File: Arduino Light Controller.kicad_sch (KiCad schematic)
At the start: 44 parts, among them J1 Terminal - Pin - Male - 1x2 -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, J10 Terminal - Pin - Male - 1x2 -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, J11 Terminal - Pin - Male - 1x2 -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, J12 Terminal - Pin - Male - 1x2 -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, J13 Terminal - Pin - Male - 1x2 -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, J14 Terminal - Pin - Male - 1x2 -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, J15 Terminal - Pin - Male - 1x2 -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, J16 Terminal - Pin - Male - 1x2 -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, J17 Terminal - Pin - Male - 1x2 -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, J18 Terminal - Pin - Male - 1x2 -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, J19 Terminal - Pin - Male - 1x4 -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, J2 Terminal - Pin - Male - 1x2 -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, J20 Terminal - Pin - Male - 1x4 -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, J21 Terminal - Pin - Male - 1x4 -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, J22 Terminal - Pin - Male - 1x4 -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, J3 Terminal - Pin - Male - 1x2 -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, J4 Terminal - Pin - Male - 1x2 -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, J5 Terminal - Pin - Male - 1x2 -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, J6 Terminal - Pin - Male - 1x2 -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, J7 Terminal - Pin - Male - 1x2 -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, J8 Terminal - Pin - Male - 1x2 -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, J9 Terminal - Pin - Male - 1x2 -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

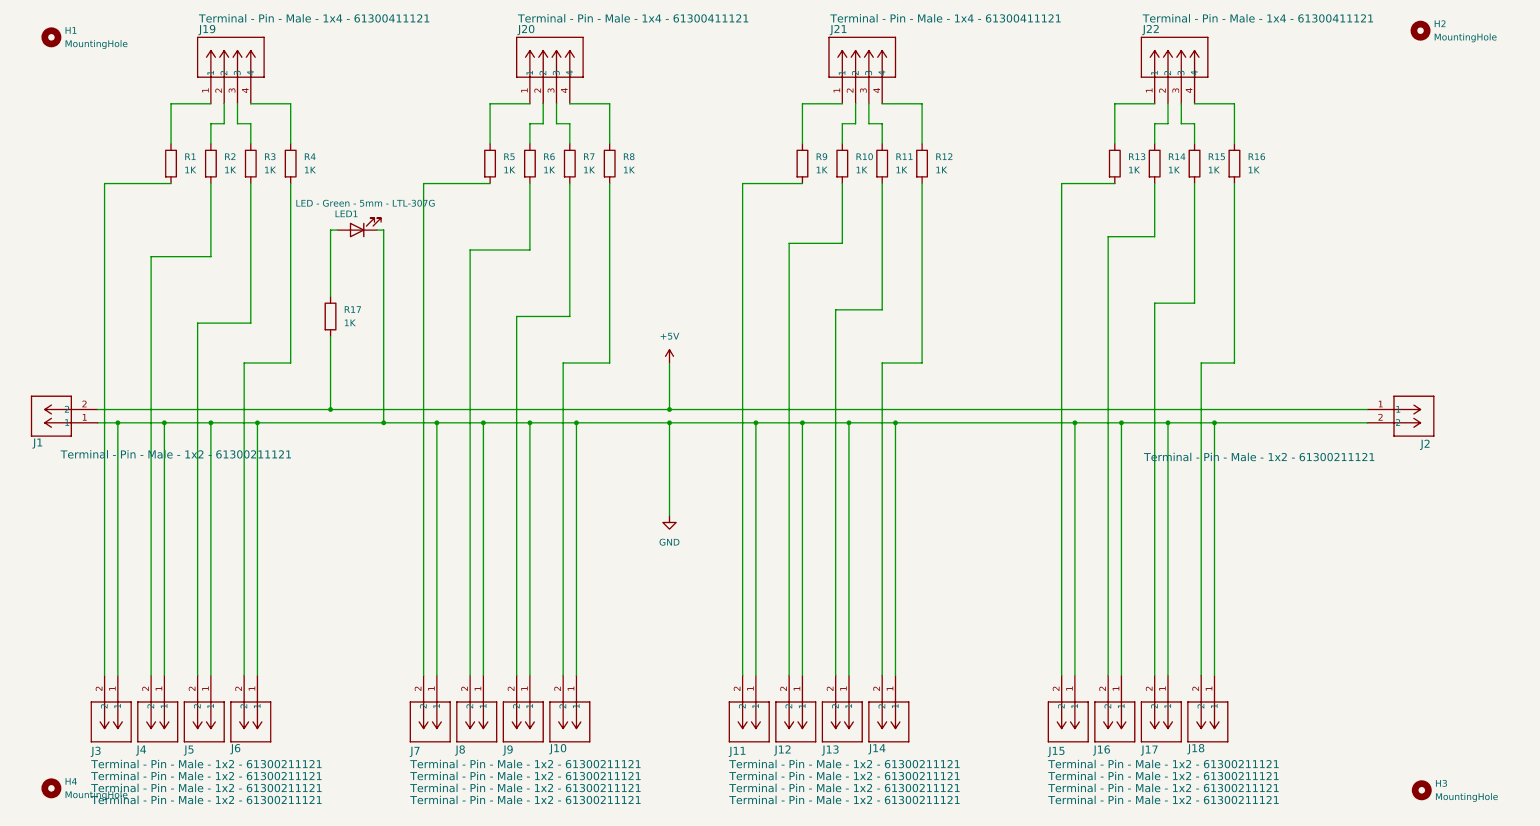
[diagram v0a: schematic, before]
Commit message: New design to align with other boards and support power bus.
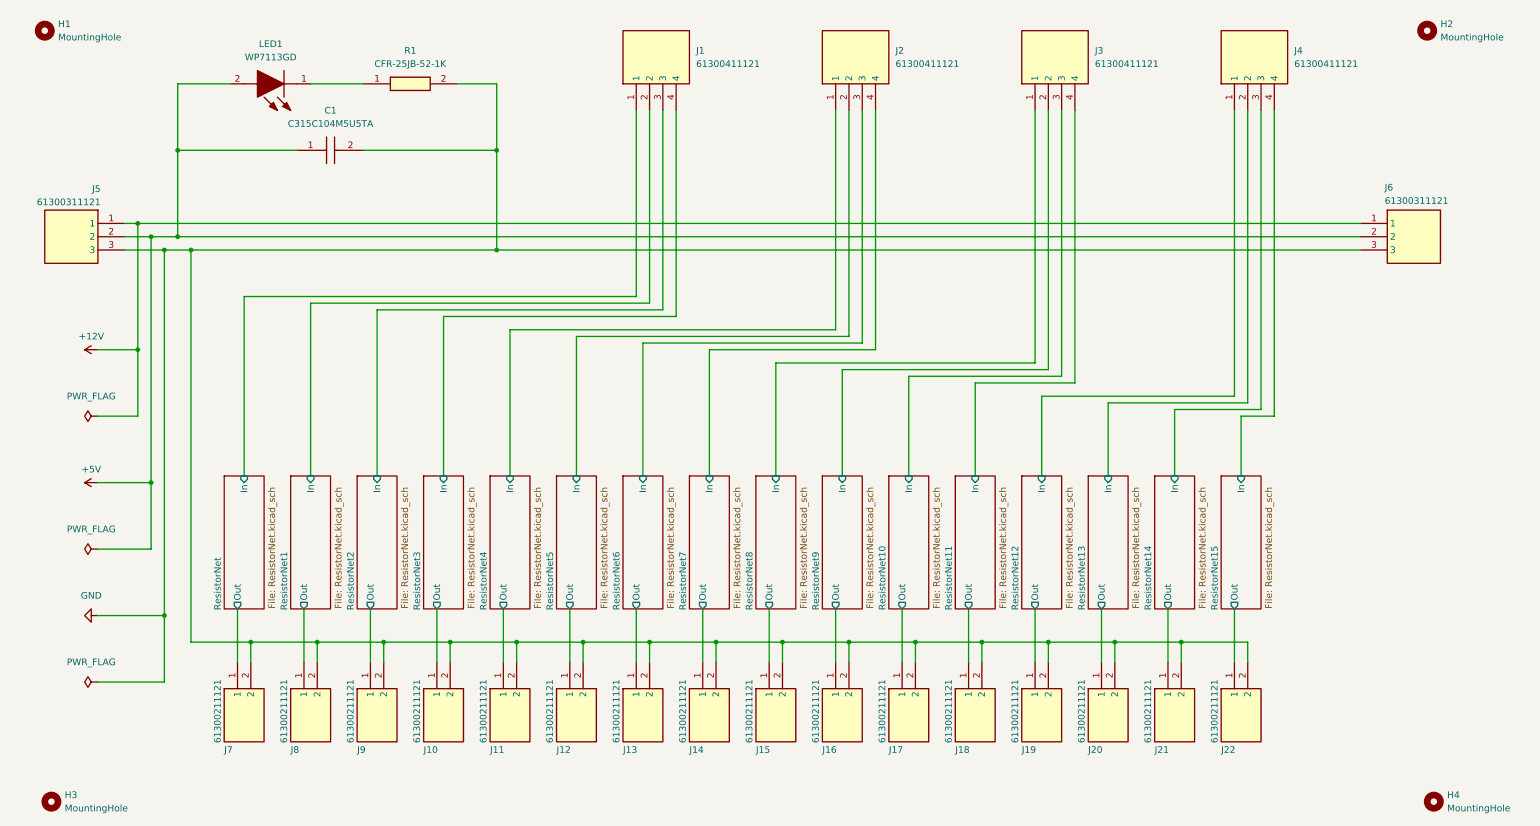
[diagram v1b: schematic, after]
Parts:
- removed J1, J10, J11, J12, J13, J14, J15, J16, J17, J18, J2, J3, J4, J5, J6, J7, J8, J9: Terminal - Pin - Male - 1x2 - 61300211121, Digikey:Terminal - Pin - Male - 1x2 - 61300211121, symbol Digikey:Terminal - Pin - Male - 1x2 - 61300211121
- removed J19, J20, J21, J22: Terminal - Pin - Male - 1x4 - 61300411121, Digikey:Terminal - Pin - Male - 1x4 - 61300411121, symbol Digikey:Terminal - Pin - Male - 1x4 - 61300411121
- removed LED1: LED - Green - 5mm - LTL-307G, Digikey:LED - Green - 5mm - LTL-307G, symbol Digikey:LED - Green - 5mm - LTL-307G
- removed R1, R10, R11, R12, R13, R14, R15, R16, R17, R2, R3, R4, R5, R6, R7, R8, R9: 1K, Resistor_THT:R_Axial_DIN0204_L3.6mm_D1.6mm_P7.62mm_Horizontal, symbol Digikey:Resistor - Generic
- added C1: C315C104M5U5TA, SamacSys_Parts:C315C100J2G5TA, symbol SamacSys_Parts:C315C104M5U5TA
- added J1, J2, J3, J4: 61300411121, SamacSys_Parts:HDRV4W95P0X254_1X4_1016X254X854P, symbol SamacSys_Parts:61300411121
- added J10, J11, J12, J13, J14, J15, J16, J17, J18, J19, J20, J21, J22, J7, J8, J9: 61300211121, SamacSys_Parts:HDRV2W110P0X254_1X2_508X254X854P, symbol SamacSys_Parts:61300211121
- added J5, J6: 61300311121, SamacSys_Parts:HDRV3W64P0X254_1X3_762X254X869P, symbol SamacSys_Parts:61300311121
- added LED1: WP7113GD, SamacSys_Parts:L53ND, symbol SamacSys_Parts:WP7113GD
- added R1: CFR-25JB-52-1K, SamacSys_Parts:RESAD1590W60L630D240, symbol SamacSys_Parts:CFR-25JB-52-1K
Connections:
- net +5V: now also C1.1, J5.2, J6.2, LED1.2 (A)
- net GND: now also C1.2, J10.2, J11.2, J12.2, J13.2, J14.2, J15.2, J16.2, J17.2, J18.2, J19.2, J20.2, J21.2, J22.2, J5.3, J6.3, J7.2, J8.2, J9.2, R1.2
- new net: LED1.1 (K), R1.1
- new net +12V: J5.1, J6.1
- new net ResistorNet/In: J1.1
- new net ResistorNet/Out: J7.1
- new net ResistorNet1/In: J1.2
- new net ResistorNet1/Out: J8.1
- new net ResistorNet10/In: J3.3
- new net ResistorNet10/Out: J17.1
- new net ResistorNet11/In: J3.4
- new net ResistorNet11/Out: J18.1
- new net ResistorNet12/In: J4.1
- new net ResistorNet12/Out: J19.1
- new net ResistorNet13/In: J4.2
- new net ResistorNet13/Out: J20.1
- new net ResistorNet14/In: J4.3
- new net ResistorNet14/Out: J21.1
- new net ResistorNet15/In: J4.4
- new net ResistorNet15/Out: J22.1
- new net ResistorNet2/In: J1.3
- new net ResistorNet2/Out: J9.1
- new net ResistorNet3/In: J1.4
- new net ResistorNet3/Out: J10.1
- new net ResistorNet4/In: J2.1
- new net ResistorNet4/Out: J11.1
- new net ResistorNet5/In: J2.2
- new net ResistorNet5/Out: J12.1
- new net ResistorNet6/In: J2.3
- new net ResistorNet6/Out: J13.1
- new net ResistorNet7/In: J2.4
- new net ResistorNet7/Out: J14.1
- new net ResistorNet8/In: J3.1
- new net ResistorNet8/Out: J15.1
- new net ResistorNet9/In: J3.2
- new net ResistorNet9/Out: J16.1
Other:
- added sheet ResistorNet (ResistorNet.kicad_sch)
- added sheet ResistorNet1 (ResistorNet.kicad_sch)
- added sheet ResistorNet10 (ResistorNet.kicad_sch)
- added sheet ResistorNet11 (ResistorNet.kicad_sch)
- added sheet ResistorNet12 (ResistorNet.kicad_sch)
- added sheet ResistorNet13 (ResistorNet.kicad_sch)
- added sheet ResistorNet14 (ResistorNet.kicad_sch)
- added sheet ResistorNet15 (ResistorNet.kicad_sch)
- added sheet ResistorNet2 (ResistorNet.kicad_sch)
- added sheet ResistorNet3 (ResistorNet.kicad_sch)
- added sheet ResistorNet4 (ResistorNet.kicad_sch)
- added sheet ResistorNet5 (ResistorNet.kicad_sch)
- added sheet ResistorNet6 (ResistorNet.kicad_sch)
- added sheet ResistorNet7 (ResistorNet.kicad_sch)
- added sheet ResistorNet8 (ResistorNet.kicad_sch)
- added sheet ResistorNet9 (ResistorNet.kicad_sch)
- moved on the sheet: H1

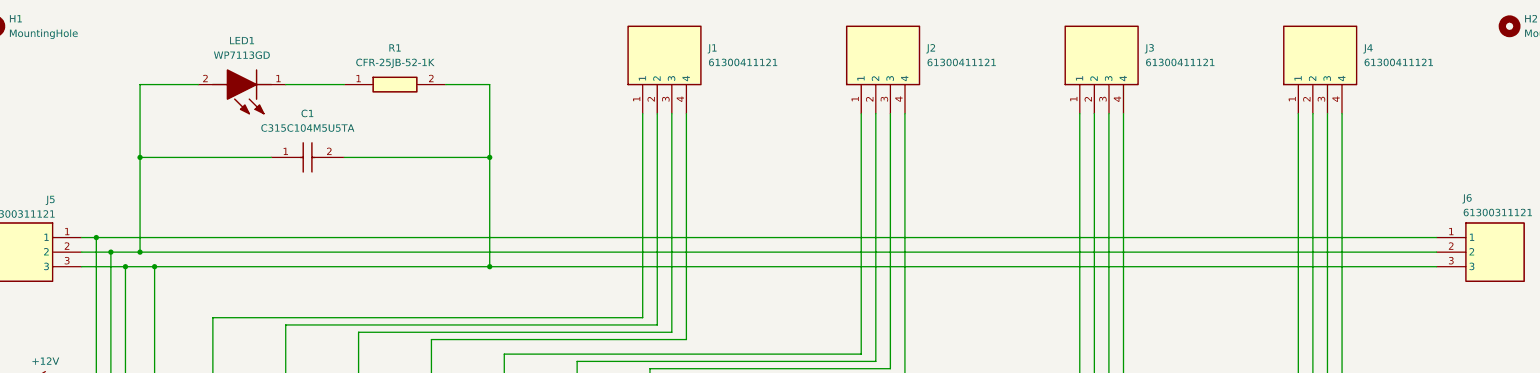
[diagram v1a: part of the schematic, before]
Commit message: Created the PowerLED subschematic and replaced the 100nF capacitor with a 10uF capacitor, added .gitignore file to ignore backups and lock file.
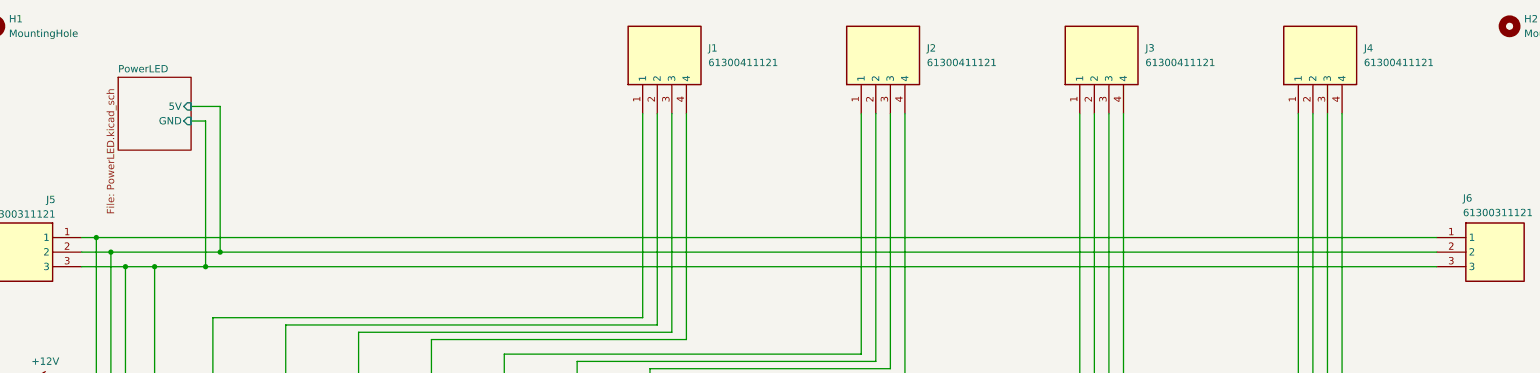
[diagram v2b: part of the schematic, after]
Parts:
- removed C1: C315C104M5U5TA, SamacSys_Parts:C315C100J2G5TA, symbol SamacSys_Parts:C315C104M5U5TA
- removed LED1: WP7113GD, SamacSys_Parts:L53ND, symbol SamacSys_Parts:WP7113GD
- removed R1: CFR-25JB-52-1K, SamacSys_Parts:RESAD1590W60L630D240, symbol SamacSys_Parts:CFR-25JB-52-1K
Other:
- added sheet PowerLED (PowerLED.kicad_sch)
